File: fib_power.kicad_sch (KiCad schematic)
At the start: 66 parts, among them Q1 PJE138K_2, Q2 PJE138K_2, U2 74LVC2G14_SOT457, U202 TLV75733PDBV, U204 TPS56428DDA, U205 TPS56428DDA, U5 TLV75733PDBV, U6 74LVC1G175_SOT457, U7 TLV75733PDBV

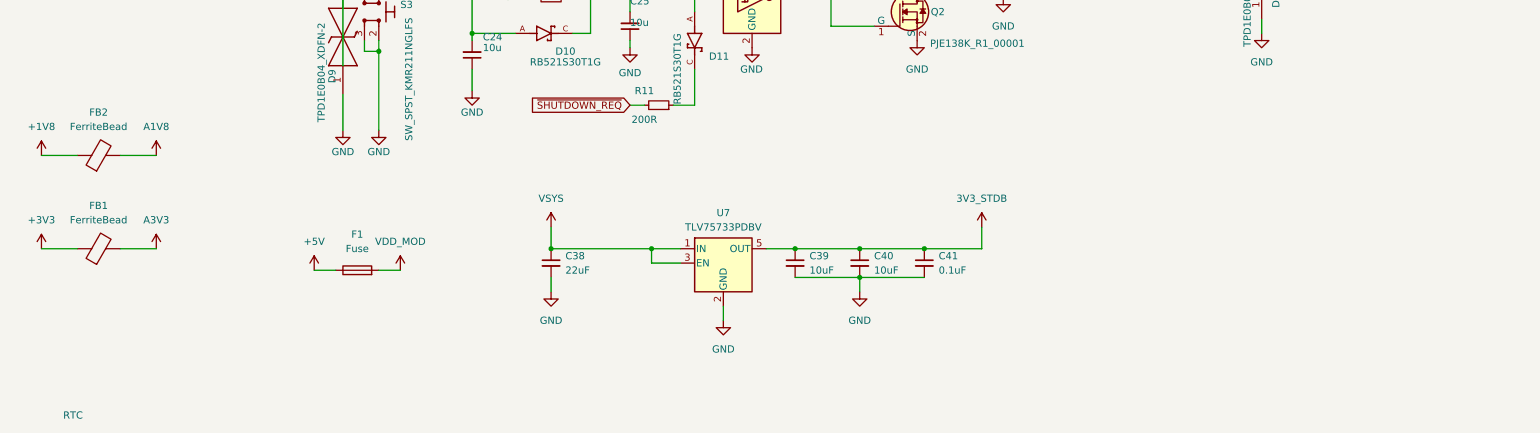
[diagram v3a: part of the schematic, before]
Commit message: added port expander and level shifters, routed peripherals fixed most drc errors, assigned gpios etc.
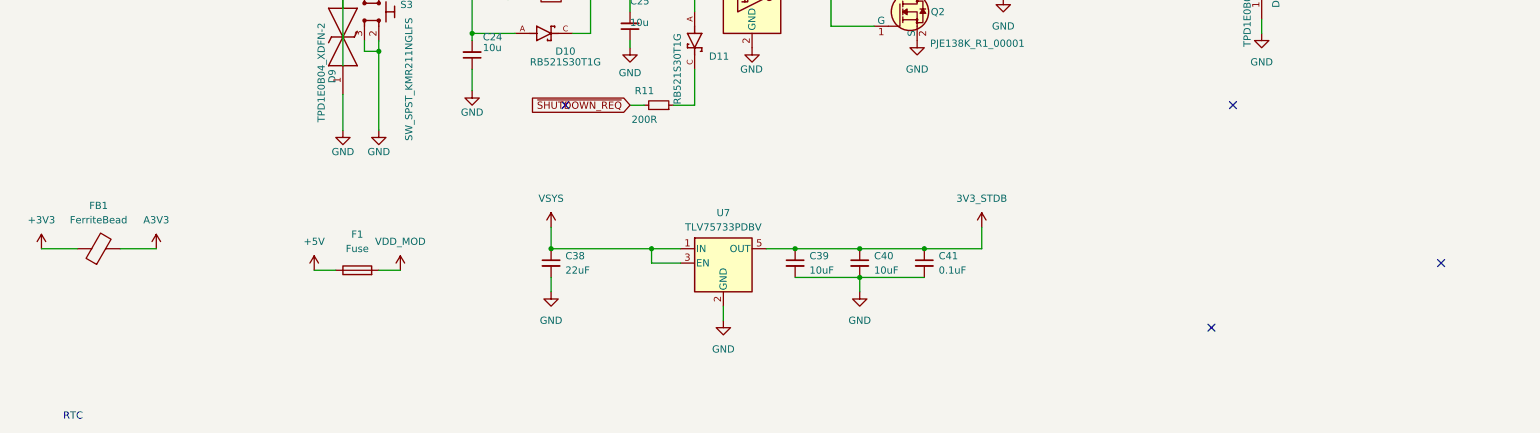
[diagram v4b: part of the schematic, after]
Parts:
- removed FB2: FerriteBead, Fibel2:Ferrite_1206, symbol Device:FerriteBead
- D8, D9: footprint TPD1E0B04DPYT -> Fibel2:TPD1E0B04DPYT
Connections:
- no-connect marks 0 -> 4
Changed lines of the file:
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@@
 		(color 0 0 0 0)
 	)
+	(no_connect
+		(at 114.3 121.92)
+	)
+	(no_connect
+		(at 228.6 161.29)
+	)
+	(no_connect
+		(at 269.24 149.86)
+	)
+	(no_connect
+		(at 232.41 121.92)
+	)
 	(wire
 		(pts
@@
 	(wire
 		(pts
-			(xy 21.59 130.81) (xy 27.94 130.81)
-		)
-		(stroke
-			(width 0)
-			(type default)
-		)
-	)
-	(wire
-		(pts
 			(xy 62.23 66.04) (xy 73.66 66.04)
 		)
@@
 	(wire
 		(pts
-			(xy 35.56 130.81) (xy 41.91 130.81)
-		)
-		(stroke
-			(width 0)
-			(type default)
-		)
-	)
-	(wire
-		(pts
 			(xy 57.15 60.96) (xy 62.23 60.96)
 		)
@@
 	)
 	(symbol
-		(lib_id "power:+3V3")
-		(at 41.91 130.81 0)
-		(unit 1)
-		(exclude_from_sim no)
-		(in_bom yes)
-		(on_board yes)
-		(dnp no)
-		(fields_autoplaced yes)
-		(property "Reference" "#PWR0211"
-			(at 41.91 134.62 0)
-			(effects
-				(font
-					(size 1.27 1.27)
-				)
-				(hide yes)
-			)
-		)
-		(property "Value" "A1V8"
-			(at 41.91 125.73 0)
-			(effects
-				(font
-					(size 1.27 1.27)
-				)
-			)
-		)
-		(property "Footprint" ""
-			(at 41.91 130.81 0)
-			(effects
-				(font
-					(size 1.27 1.27)
-				)
-				(hide yes)
-			)
-		)
-		(property "Datasheet" ""
-			(at 41.91 130.81 0)
-			(effects
-				(font
-					(size 1.27 1.27)
-				)
-				(hide yes)
-			)
-		)
-		(property "Description" "Power symbol creates a global label with name \"+3V3\""
-			(at 41.91 130.81 0)
-			(effects
-				(font
-					(size 1.27 1.27)
-				)
-				(hide yes)
-			)
-		)
-		(pin "1"
-		)
-		(instances
-			(project "Fibel2"
-				(path "/862c21e2-7ec9-4f80-a33c-aad02ea9423e/7cbf83a4-48a9-4119-ac75-03df93e67514"
-					(reference "#PWR0211")
-					(unit 1)
-				)
-			)
-		)
-	)
-	(symbol
 		(lib_id "Fibel2:TPD1E0B04DPYT")
 		(at 74.93 120.015 90)
@@
 			)
 		)
-		(property "Footprint" "TPD1E0B04DPYT"
+		(property "Footprint" "Fibel2:TPD1E0B04DPYT"
 			(at 168.58 107.315 0)
 			(effects
@@
 	)
 	(symbol
-		(lib_id "power:+1V8")
-		(at 21.59 130.81 0)
-		(unit 1)
-		(exclude_from_sim no)
-		(in_bom yes)
-		(on_board yes)
-		(dnp no)
-		(fields_autoplaced yes)
-		(property "Reference" "#PWR0227"
-			(at 21.59 134.62 0)
-			(effects
-				(font
-					(size 1.27 1.27)
-				)
-				(hide yes)
-			)
-		)
-		(property "Value" "+1V8"
-			(at 21.59 125.73 0)
-			(effects
-				(font
-					(size 1.27 1.27)
-				)
-			)
-		)
-		(property "Footprint" ""
-			(at 21.59 130.81 0)
-			(effects
-				(font
-					(size 1.27 1.27)
-				)
-				(hide yes)
-			)
-		)
-		(property "Datasheet" ""
-			(at 21.59 130.81 0)
-			(effects
-				(font
-					(size 1.27 1.27)
-				)
-				(hide yes)
-			)
-		)
-		(property "Description" "Power symbol creates a global label with name \"+1V8\""
-			(at 21.59 130.81 0)
-			(effects
-				(font
-					(size 1.27 1.27)
-				)
-				(hide yes)
-			)
-		)
-		(pin "1"
-		)
-		(instances
-			(project "Fibel2"
-				(path "/862c21e2-7ec9-4f80-a33c-aad02ea9423e/7cbf83a4-48a9-4119-ac75-03df93e67514"
-					(reference "#PWR0227")
-					(unit 1)
-				)
-			)
-		)
-	)
-	(symbol
 		(lib_id "power:VCC")
 		(at 270.51 21.59 0)
@@
 			)
 		)
-		(property "Footprint" "TPD1E0B04DPYT"
+		(property "Footprint" "Fibel2:TPD1E0B04DPYT"
 			(at 331.14 93.98 0)
 			(effects
@@
 					(unit 1)
 				)
-			)
-		)
-	)
-	(symbol
-		(lib_id "Device:FerriteBead")
-		(at 31.75 130.81 90)
-		(unit 1)
-		(exclude_from_sim no)
-		(in_bom yes)
-		(on_board yes)
-		(dnp no)
-		(fields_autoplaced yes)
-		(property "Reference" "FB2"
-			(at 31.6992 123.19 90)
-			(effects
-				(font
-					(size 1.27 1.27)
-				)
-			)
-		)
-		(property "Value" "FerriteBead"
-			(at 31.6992 125.73 90)
-			(effects
-				(font
-					(size 1.27 1.27)
-				)
-			)
-		)
-		(property "Footprint" "Fibel2:Ferrite_1206"
-			(at 31.75 132.588 90)
-			(effects
-				(font
-					(size 1.27 1.27)
-				)
-				(hide yes)
-			)
-		)
-		(property "Datasheet" "~"
-			(at 31.75 130.81 0)
-			(effects
-				(font
-					(size 1.27 1.27)
-				)
-				(hide yes)
-			)
-		)
-		(property "Description" "Ferrite bead"
-			(at 31.75 130.81 0)
-			(effects
-				(font
-					(size 1.27 1.27)
-				)
-				(hide yes)
-			)
-		)
-		(pin "2"
-		)
-		(pin "1"
-		)
-		(instances
-			(project "Fibel2"
-				(path "/862c21e2-7ec9-4f80-a33c-aad02ea9423e/7cbf83a4-48a9-4119-ac75-03df93e67514"
-					(reference "FB2")
-					(unit 1)
-				)

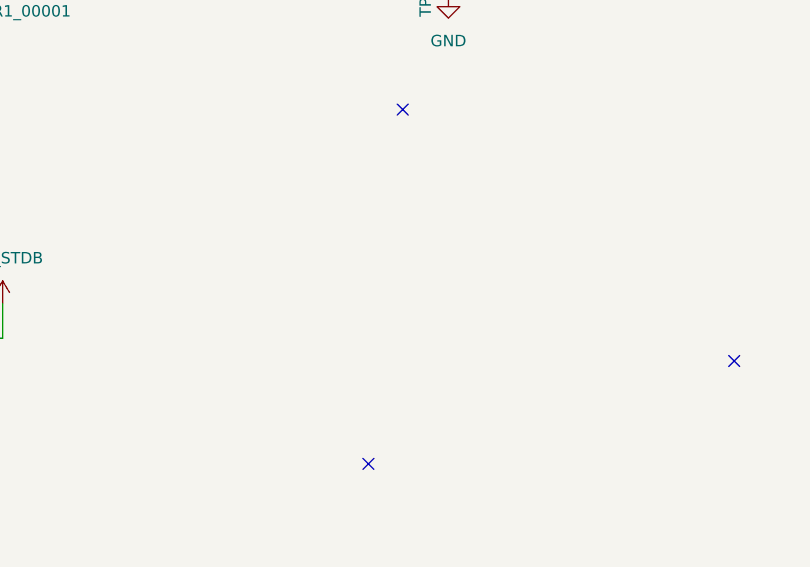
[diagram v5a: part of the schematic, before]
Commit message: added second i2c, modified 40 pin headers
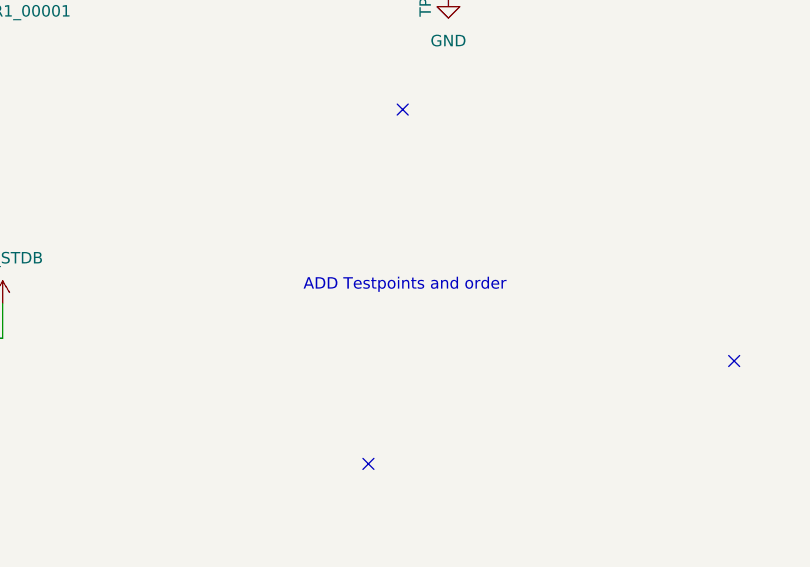
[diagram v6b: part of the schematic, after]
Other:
- note added: "ADD Testpoints and order"
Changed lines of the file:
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@@
 		)
 	)
+	(text "ADD Testpoints and order"
+		(exclude_from_sim no)
+		(at 232.664 141.478 0)
+		(effects
+			(font
+				(size 1.27 1.27)
+			)
+		)
+	)
 	(text "1V8\n"
 		(exclude_from_sim no)
@@
 		)
 		(instances
-			(project ""
+			(project "Fibel2"
 				(path "/862c21e2-7ec9-4f80-a33c-aad02ea9423e/7cbf83a4-48a9-4119-ac75-03df93e67514"
 					(reference "F1")
@@
 		)
 		(instances
-			(project ""
+			(project "Fibel2"
 				(path "/862c21e2-7ec9-4f80-a33c-aad02ea9423e/7cbf83a4-48a9-4119-ac75-03df93e67514"
 					(reference "FB1")

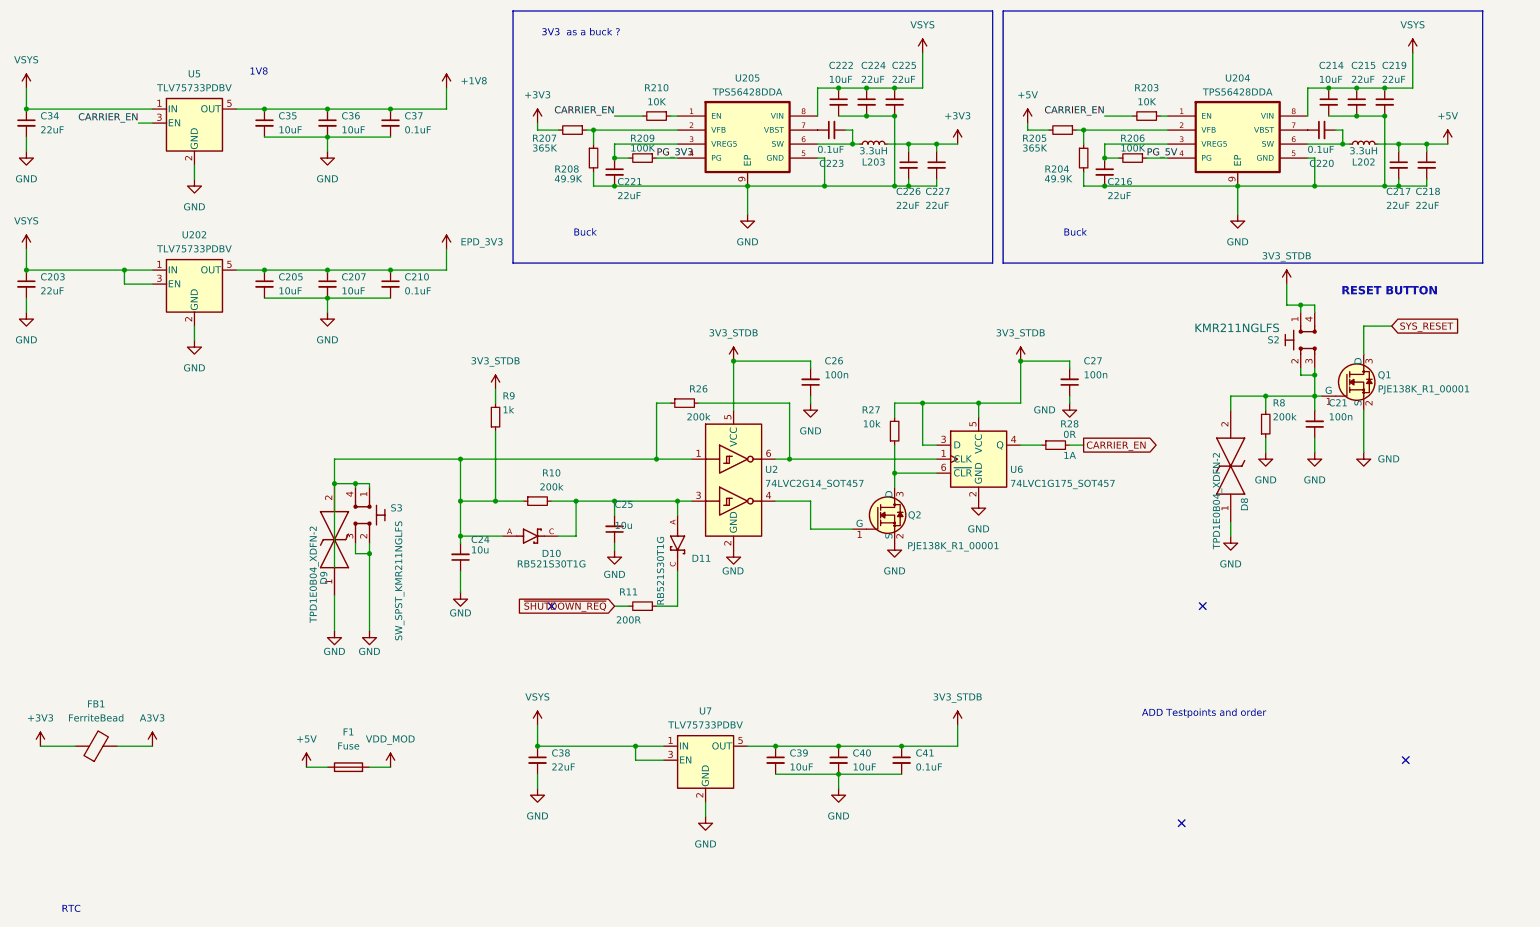
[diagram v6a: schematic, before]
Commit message: adde testpoints, fixed power supplies, ready to order
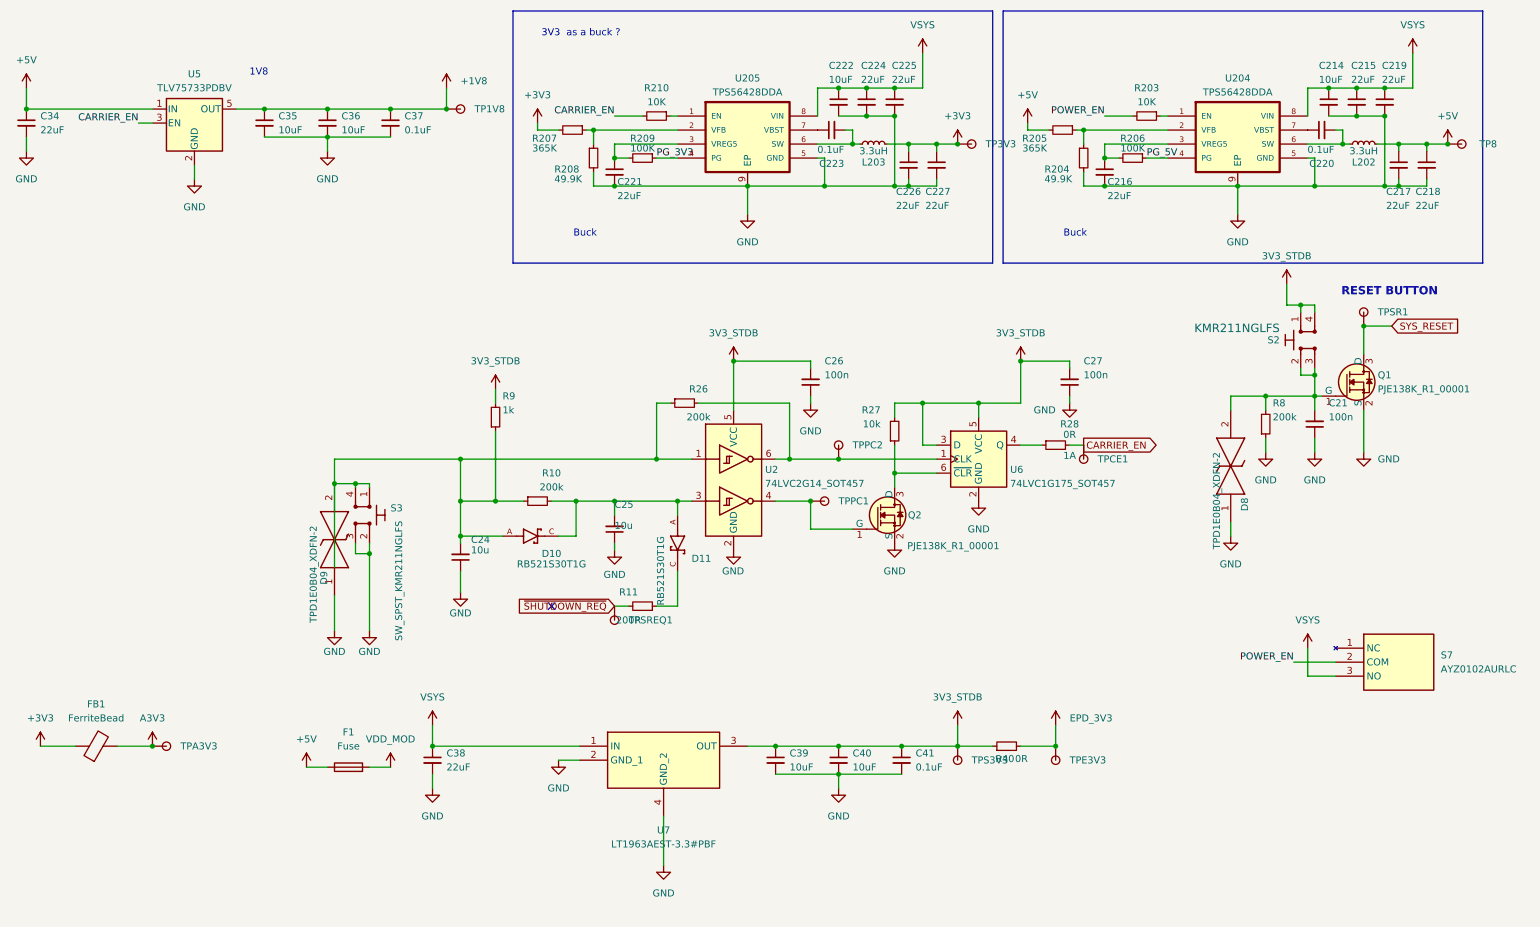
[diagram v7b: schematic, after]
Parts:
- removed C203: 22uF, Capacitor_SMD:C_0805_2012Metric, symbol Device:C_Small
- removed C205, C207: 10uF, Capacitor_SMD:C_0603_1608Metric, symbol Device:C_Small
- removed C210: 0.1uF, Capacitor_SMD:C_0402_1005Metric, symbol Device:C_Small
- removed U202, U7: TLV75733PDBV, Package_TO_SOT_SMD:SOT-23-5, symbol Regulator_Linear:TLV75733PDBV
- added R40: 0R, Resistor_SMD:R_0603_1608Metric, symbol Device:R_Small
- added S7: AYZ0102AURLC, AYZ0102AURLC, symbol Fibel2:AYZ0102AURLC
- added TP1V8, TP3V3, TP8, TPA3V3, TPCE1, TPE3V3, TPPC1, TPPC2, TPS3V3, TPSR1, TPSREQ1: TestPoint, TestPoint:TestPoint_Pad_D1.0mm, symbol Fibel2:TestPoint
- added U7: LT1963AEST-3.3#PBF, SOT230P700X180-4N, symbol Fibel2:LT1963AEST-3.3#PBF
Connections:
- net +1V8: now also TP1V8.1
- net +3V3: now also TP3V3.1
- net +5V: now also C34.1, U5.1 (IN), TP8.1
- net 3V3_STDB: now also R40.1, TPS3V3.1, U7.3 (OUT)
- net A3V3: now also TPA3V3.1
- net CARRIER_EN: now also TPCE1.1; no longer R203.2
- net EPD_3V3: now also R40.2, TPE3V3.1
- net GND: now also U7.2 (GND_1), U7.4 (GND_2)
- net SYS_RESET: now also TPSR1.1
- net VSYS: now also S7.3 (NO), U7.1 (IN); no longer C34.1, U5.1 (IN)
- net ~{SHUTDOWN_REQ}: now also TPSREQ1.1
- net at R26.2, U2.6, U6.1 (CLK): now also TPPC2.1
- net at Q2.1 (G), U2.4: now also TPPC1.1
- new net POWER_EN: R203.2, S7.2 (COM)
- no-connect marks 4 -> 1
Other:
- note removed: "ADD Testpoints and order"
- note removed: "RTC"
- moved on the sheet: C38
